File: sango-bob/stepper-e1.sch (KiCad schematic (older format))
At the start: 26 parts, among them P901 CONN_8, P902 CONN_8, P903 MOT_E1, U901 A4985-LP

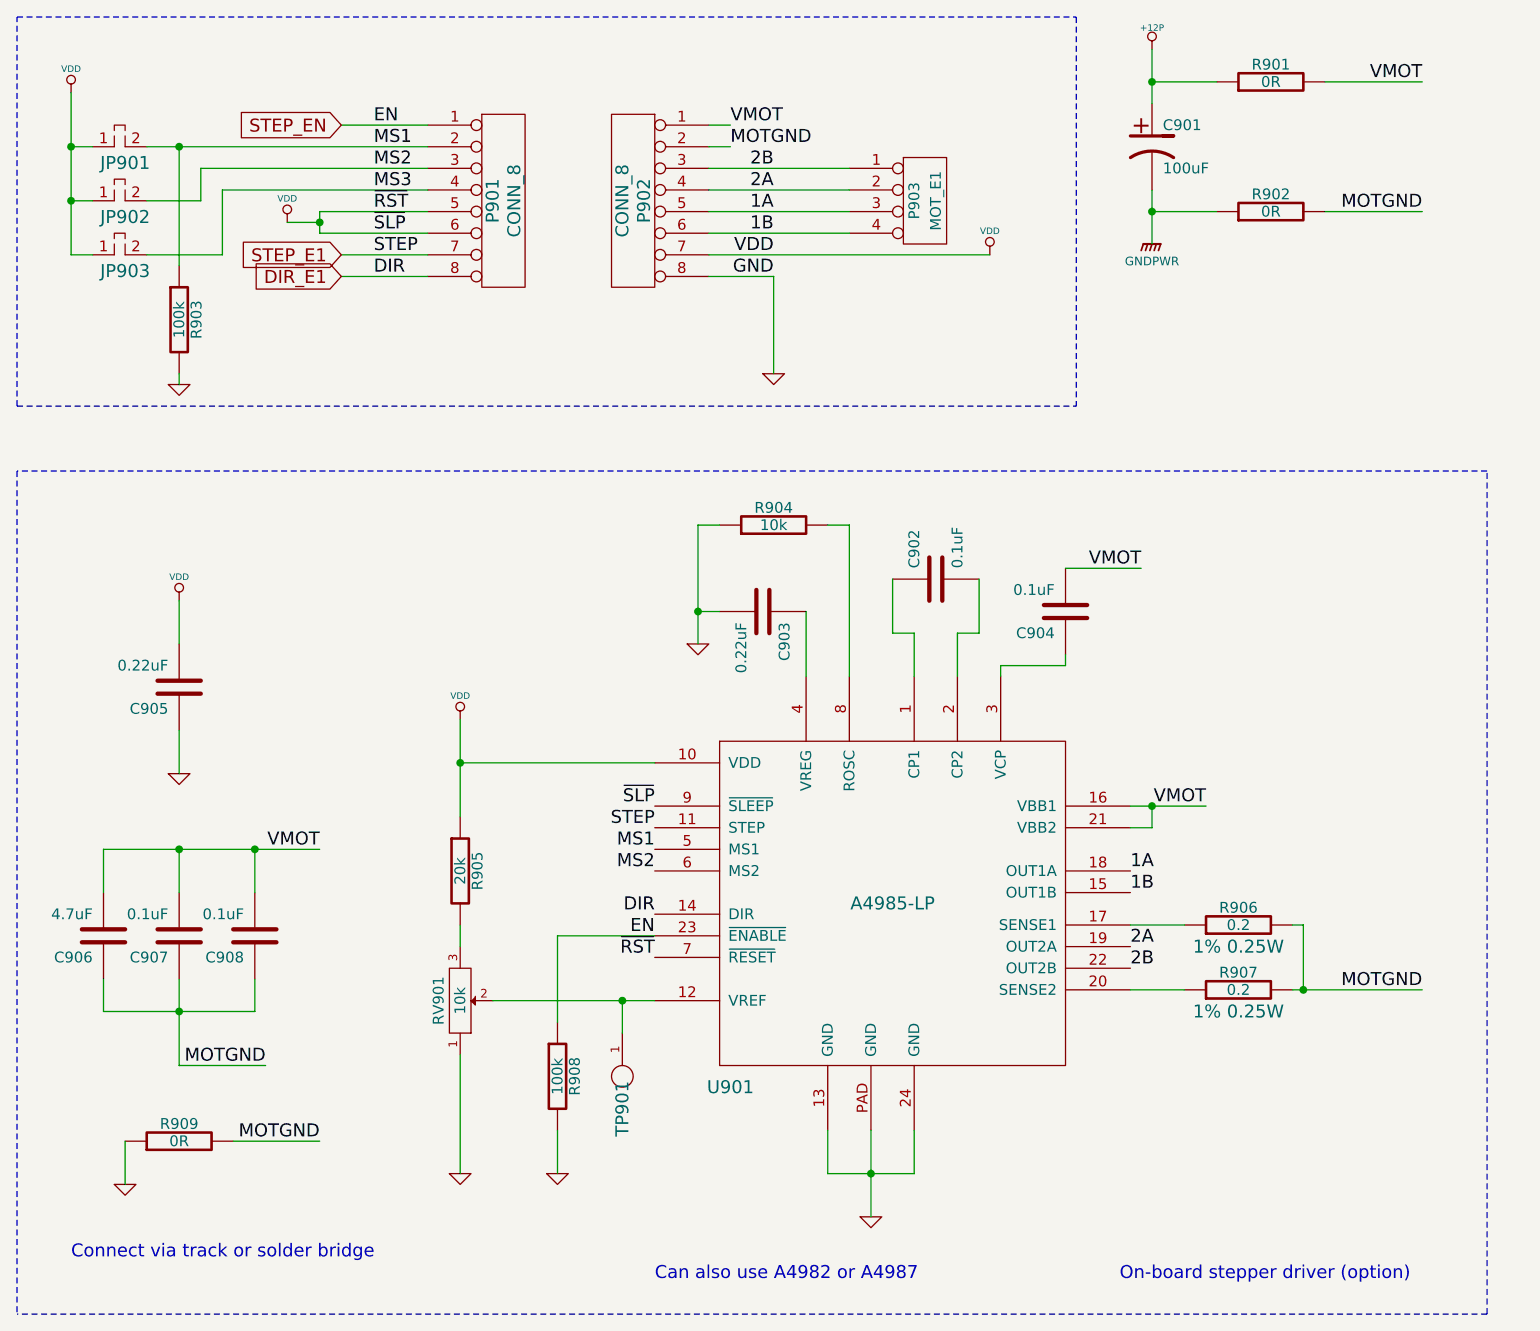
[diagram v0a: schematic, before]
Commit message: Updates to symbols and fix some ERC errors
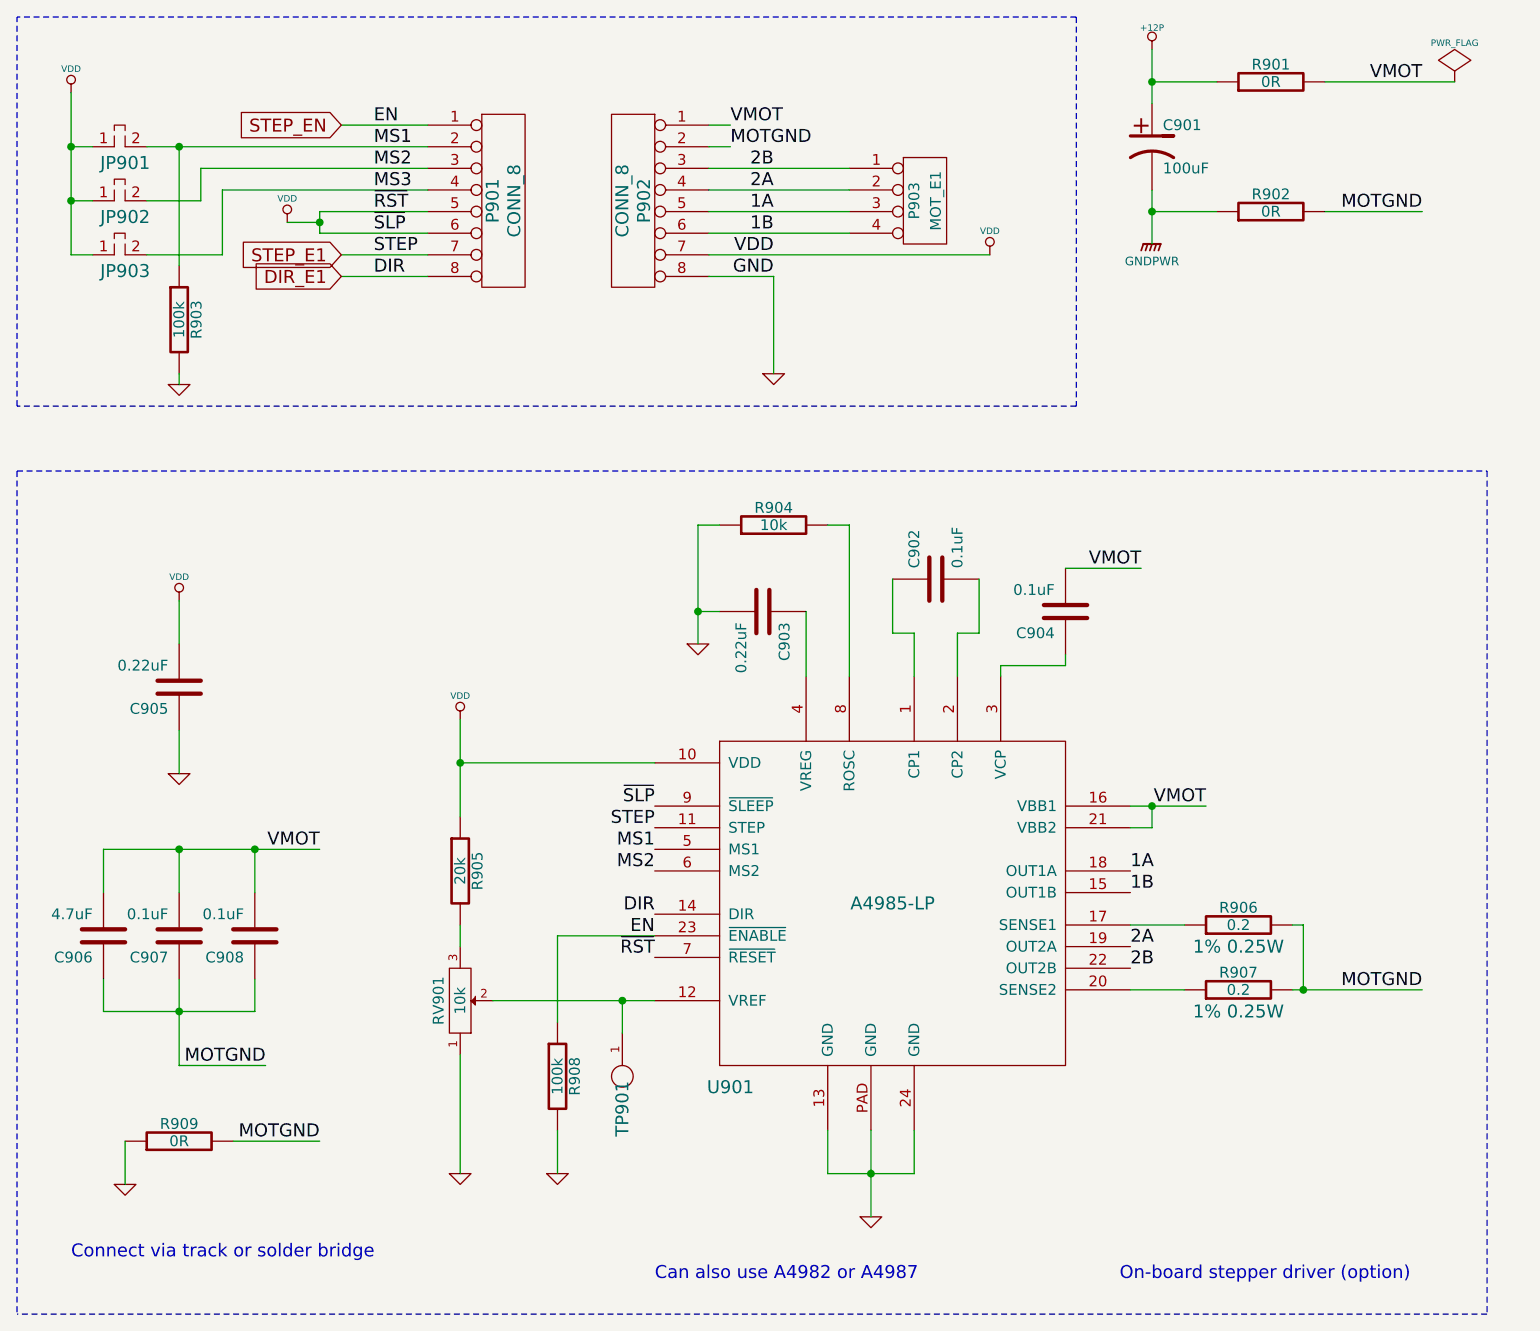
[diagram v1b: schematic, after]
